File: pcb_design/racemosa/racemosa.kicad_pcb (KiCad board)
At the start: 2 copper layers, 46.5 x 93 mm, 4 parts, among them J1 USB_C_Receptacle, J2 USB_C_Receptacle, J3 Conn_02x16_Odd_Even

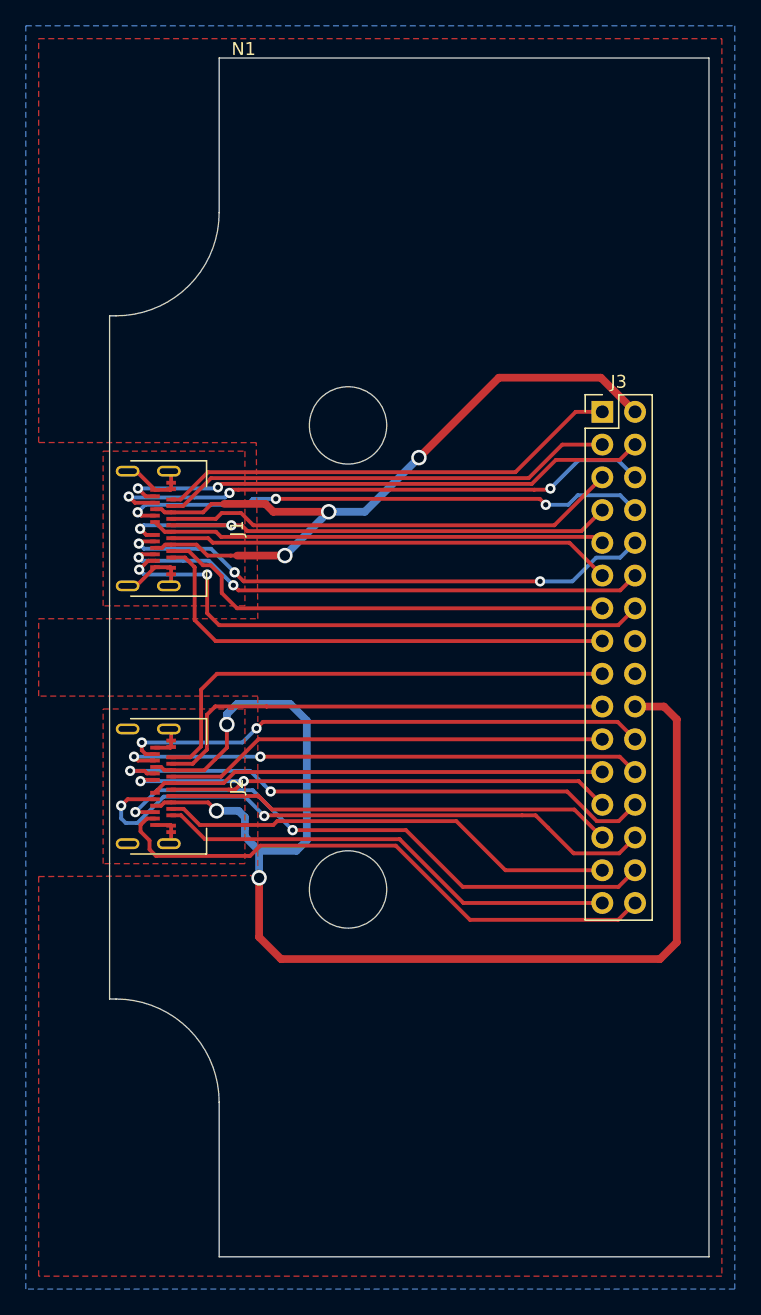
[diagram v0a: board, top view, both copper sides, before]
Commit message: Redesign for improved mounting hole placement.
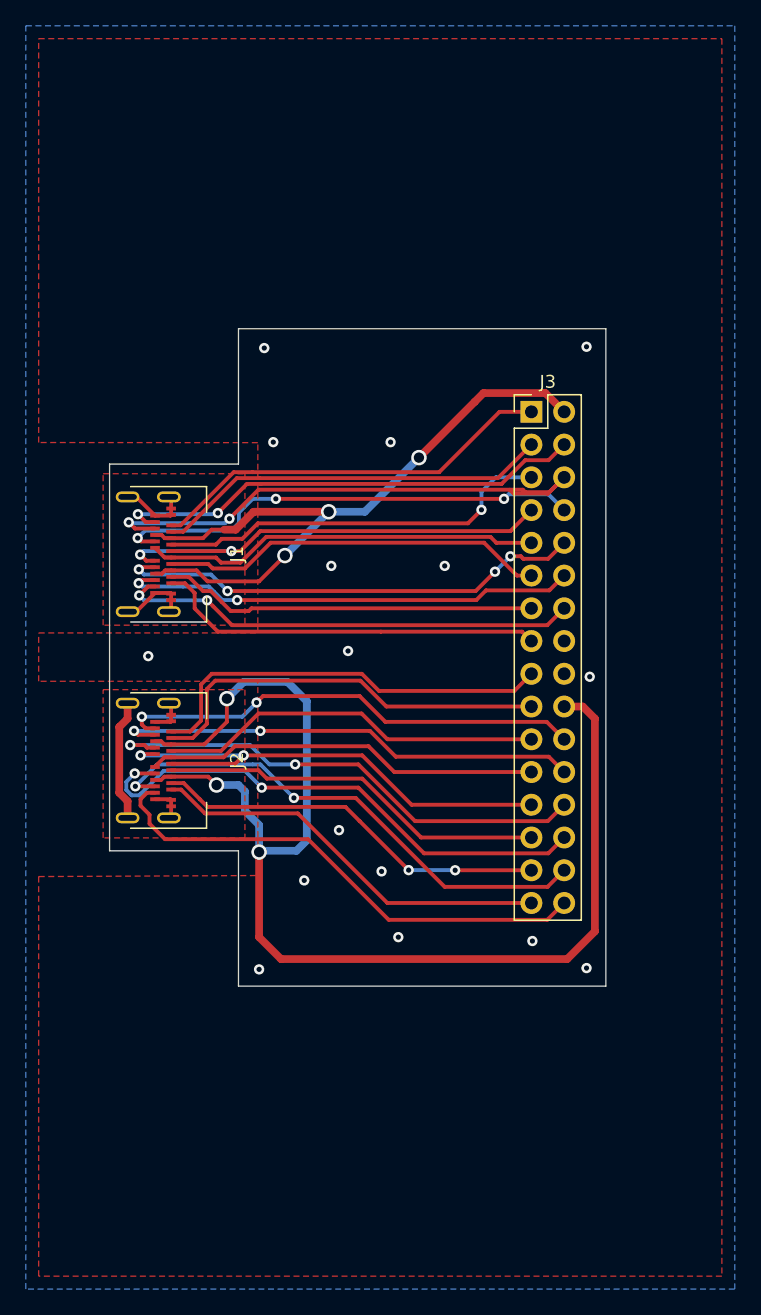
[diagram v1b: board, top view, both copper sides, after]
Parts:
- N1: footprint custom_footprints:Enclosure-Gloxinia_small -> custom_footprints:Enclosure-Gloxinia2_lr
- moved N1 19.2 mm to (92.8, 85.0)
- moved J3 5.50 mm to (98.2, 66.0)
- moved J1 2.00 mm to (69.0, 77.0)
- moved J2 2.00 mm to (69.0, 93.0)
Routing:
- net GND: track 16.4 -> 25.9 mm, vias 0 -> 16
- net /TX2+1: track 44.1 -> 36.0 mm
- net /RX2+1: track 38.5 -> 30.5 mm
- net /RX2-1: track 36.1 -> 29.1 mm
- net /TX1+2: track 38.7 -> 32.5 mm
- net /CC22: track 47.1 -> 41.2 mm
- net /TX2-1: track 41.4 -> 35.7 mm
- net /CC21: track 42.3 -> 36.7 mm, vias 3 -> 4
- net /VBUS1: track 58.6 -> 53.3 mm
- net /TX2+2: track 44.7 -> 39.3 mm
- net /D+1: track 42.9 -> 37.8 mm
- net /RX2-2: track 35.7 -> 30.8 mm, vias 0 -> 2
- net /VBUS2: track 101.3 -> 96.6 mm
- net /TX2-2: track 44.6 -> 40.0 mm
- net /TX1-2: track 36.9 -> 32.2 mm
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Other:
- board size 46.5 x 93 mm -> 38.5 x 51 mm
